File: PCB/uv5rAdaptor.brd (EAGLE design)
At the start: 100 x 80 mm, 2 parts

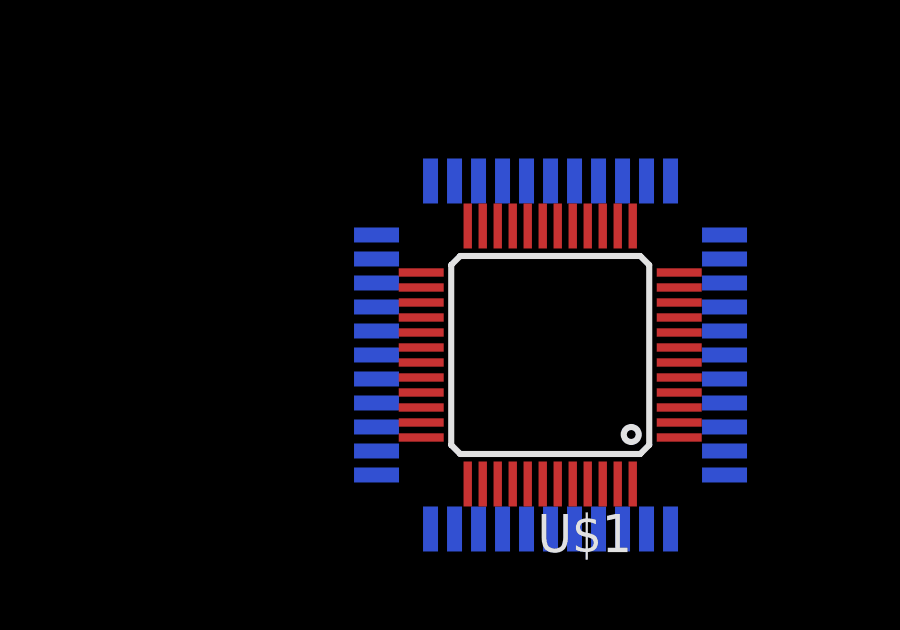
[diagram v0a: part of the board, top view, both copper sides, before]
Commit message: Link all points except for gpio6, we will do that once everything is routed
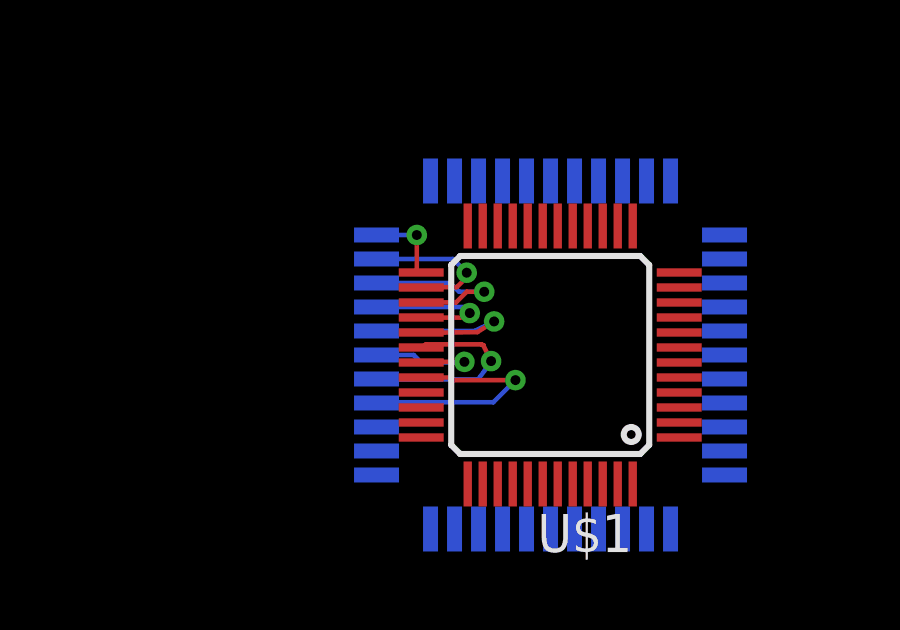
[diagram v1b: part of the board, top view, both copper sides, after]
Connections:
- net N$43 renamed NC1
- net N$45 renamed NC2
- removed net N$1: U$1.1
- removed net N$10: U$1.10
- removed net N$11: U$1.11
- removed net N$12: U$1.12
- removed net N$13: U$1.13
- removed net N$16: U$1.16
- removed net N$17: U$1.17
- removed net N$18: U$1.18
- removed net N$19: U$1.19
- removed net N$20: U$1.20
- removed net N$21: U$1.21
- removed net N$22: U$1.22
- removed net N$30: U$1.25
- removed net N$31: U$1.26
- removed net N$32: U$1.27
- removed net N$33: U$1.28
- removed net N$34: U$1.29
- removed net N$35: U$1.30
- removed net N$36: U$1.31
- removed net N$37: U$1.32
- removed net N$38: U$1.33
- removed net N$39: U$1.34
- removed net N$42: U$1.37
- removed net N$46: U$1.41
- removed net N$48: U$1.43
- new net NC11: U$1.46
- net CLK_FM: now also U$1.18
- net DATA_FM: now also U$1.32
- net GPIO0: now also U$1.17
- net GREEN_LED: now also U$1.43
- net KEY_C4: now also U$1.20; no longer U$1.46
- net KEY_COL1: now also U$1.25
- net KEY_COL2: now also U$1.26; no longer U$1.2
- net KEY_COL3: now also U$1.27; no longer U$1.3
- net LCD_CE: now also U$1.34
- net LCD_DB4: now also U$1.28; no longer U$1.4
- net LCD_DB5: now also U$1.29
- net LCD_RS: now also U$1.33
- net LOW_BAT: now also U$1.1
- net RDX/PPT: now also U$1.22
- net RED_LED: now also U$1.37
- net RX_LED: now also U$1.12
- net RX_PW: now also U$1.19
- net SCK_EEPROM: now also U$1.13
- net SCL_VOICE: now also U$1.16
- net SDA_VOICE: now also U$1.11
- net SDR_SCK: now also U$1.30
- net SDR_SDIO: now also U$1.31
- net SEN: now also U$1.10
- net SPK_AMP: now also U$1.3
- net TXD: now also U$1.21
- net TX_PW: now also U$1.2
- net UHF/VHF: now also U$1.41
- net VOX: now also U$1.4
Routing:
- net DATA_FM: track 0.00 -> 8.13 mm, vias 0 -> 1
- net SDR_SCK: track 0.00 -> 6.85 mm, vias 0 -> 1
- net LCD_DB5: track 0.00 -> 6.53 mm, vias 0 -> 1
- net KEY_COL3: track 0.00 -> 5.99 mm, vias 0 -> 1
- net LCD_DB4: track 0.00 -> 5.16 mm, vias 0 -> 1
- net KEY_COL2: track 0.00 -> 5.00 mm, vias 0 -> 1
- net SDR_SDIO: track 0.00 -> 4.49 mm, vias 0 -> 1
- net KEY_COL1: track 0.00 -> 2.74 mm, vias 0 -> 1

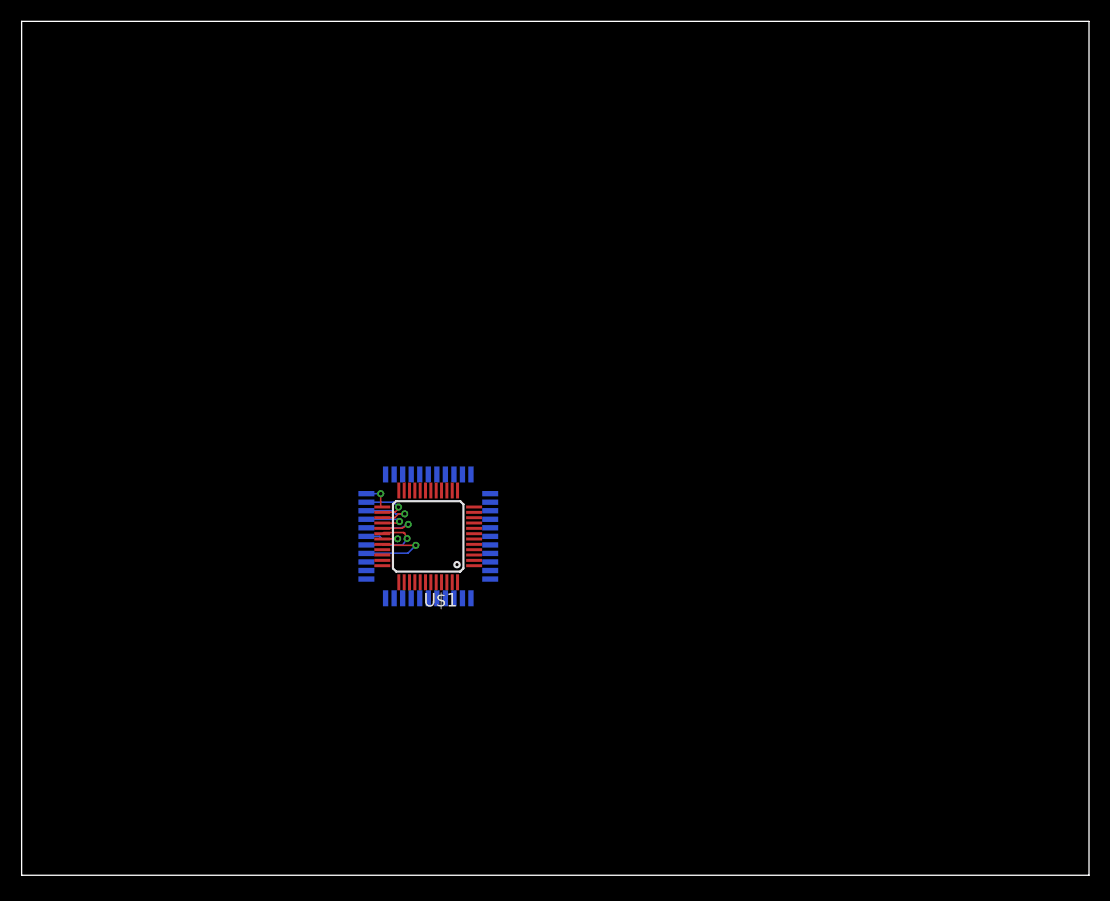
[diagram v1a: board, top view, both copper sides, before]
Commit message: Updated dims
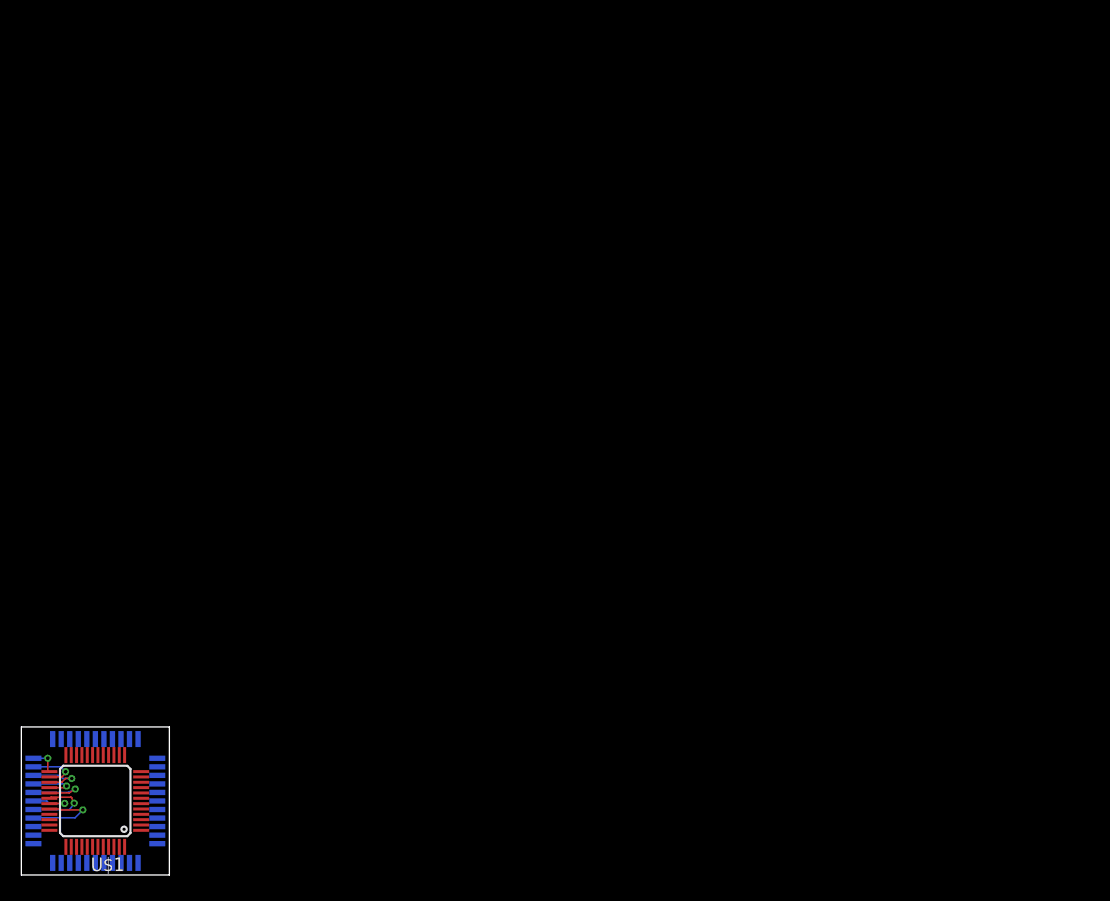
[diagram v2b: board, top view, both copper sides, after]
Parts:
- moved U$1 39.8 mm to (6.90, 6.96)
- moved U$2 39.8 mm to (6.91, 6.96)
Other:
- board size 100 x 80 mm -> 13.9 x 13.9 mm

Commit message: More routing
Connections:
- removed net N$50: U$1.45
- removed net NC1: U$1.38
- removed net NC11: U$1.46
- new net NC3: U$1.2
- new net NC4: U$1.3
- net LED_FL: now also U$1.38
- net SPK_AMP: now also U$1.46; no longer U$1.3
- net TX_PW: now also U$1.45; no longer U$1.2
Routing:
- net RESET: track 0.00 -> 8.11 mm, vias 0 -> 1
- net LCD_RS: track 0.00 -> 7.54 mm, vias 0 -> 1
- net OSC_IN: track 0.00 -> 7.31 mm, vias 0 -> 1
- net OSC_OUT: track 0.00 -> 7.25 mm, vias 0 -> 1
- net TX_PW: track 0.00 -> 6.69 mm, vias 0 -> 1
- net UHF/VHF: track 0.00 -> 6.33 mm, vias 0 -> 1
- net GREEN_LED: track 0.00 -> 6.32 mm, vias 0 -> 1
- net SPK_AMP: track 0.00 -> 6.21 mm, vias 0 -> 1
- net LCD_CE: track 0.00 -> 6.08 mm, vias 0 -> 1
- net VOX: track 0.00 -> 5.76 mm, vias 0 -> 1
- net LOW_BAT: track 0.00 -> 5.51 mm, vias 0 -> 1
- net LED_FL: track 0.00 -> 5.09 mm, vias 0 -> 1
- net RED_LED: track 0.00 -> 3.17 mm, vias 0 -> 1
- net SEN: track 0.00 -> 1.39 mm

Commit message: More traces
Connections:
- net KEY_C4: now also U$1.19; no longer U$1.20
- net RX_PW: now also U$1.20; no longer U$1.19
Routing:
- net VSS: track 0.00 -> 31.4 mm, vias 0 -> 4
- net VDD: track 0.00 -> 24.9 mm, vias 0 -> 1
- net TX_BIAS: track 0.00 -> 16.3 mm, vias 0 -> 1
- net TONE: track 0.00 -> 12.7 mm, vias 0 -> 1
- net GPIO0: track 0.00 -> 9.03 mm, vias 0 -> 1
- net CLK_FM: track 0.00 -> 8.82 mm, vias 0 -> 1
- net AVDD: track 0.00 -> 8.61 mm
- net AVSS: track 0.00 -> 8.36 mm, vias 0 -> 1
- net GREEN_LED: track 6.32 -> 7.99 mm
- net OSC_IN: track 7.31 -> 6.28 mm
- net RESET: track 8.11 -> 7.11 mm

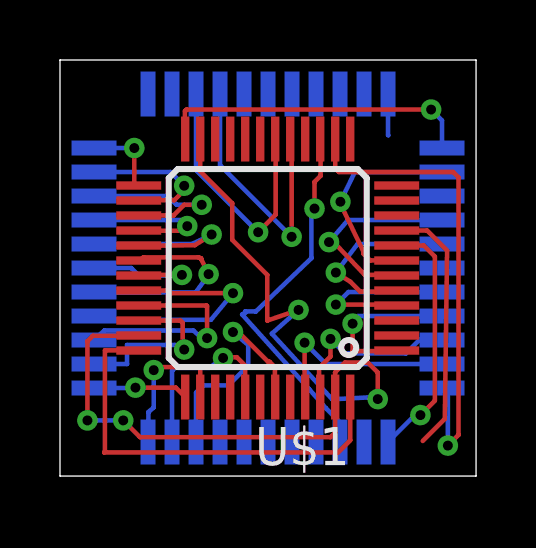
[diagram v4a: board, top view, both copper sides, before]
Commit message: Finished Routing
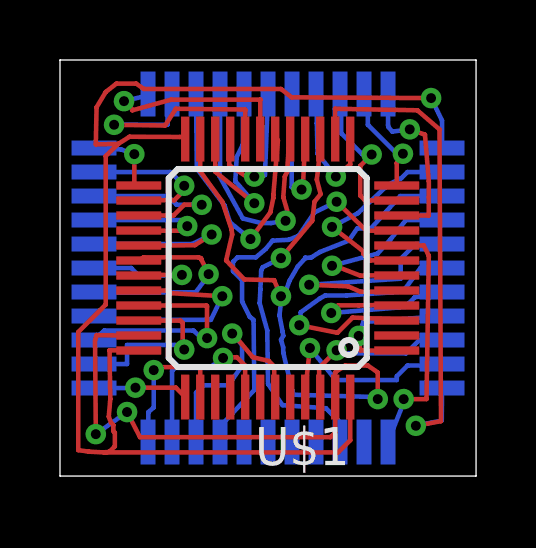
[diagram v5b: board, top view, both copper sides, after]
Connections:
- removed net N$49: U$1.44
- removed net NC3: U$1.2
- new net NC1: U$1.2
- net GPIO6: now also U$1.3
- net NC2: now also U$1.44; no longer U$1.40
- net NC4: now also U$1.40; no longer U$1.3
- net RX_LED: now also U$1.11; no longer U$1.12
- net SDA_VOICE: now also U$1.12; no longer U$1.11
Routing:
- net VDD: track 24.9 -> 43.9 mm
- net GPIO6: track 0.00 -> 9.21 mm, vias 0 -> 1
- net RX_PW: track 0.00 -> 8.52 mm, vias 0 -> 1
- net KEY_C4: track 0.00 -> 6.98 mm, vias 0 -> 1
- net VSS: track 31.4 -> 38.1 mm
- net RDX/PPT: track 0.00 -> 6.71 mm, vias 0 -> 1
- net RX_LED: track 0.00 -> 5.44 mm, vias 0 -> 1
- net SCL_VOICE: track 0.00 -> 5.16 mm, vias 0 -> 1
- net TXD: track 0.00 -> 5.00 mm, vias 0 -> 1
- net AVDD: track 8.61 -> 13.5 mm, vias 0 -> 1
- net SEN: track 1.39 -> 6.20 mm, vias 0 -> 1
- net SCK_EEPROM: track 0.00 -> 4.45 mm, vias 0 -> 1
- net SDA_VOICE: track 0.00 -> 3.85 mm, vias 0 -> 1
- net OSC_IN: track 6.28 -> 8.27 mm
- net TX_BIAS: track 16.3 -> 17.3 mm
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
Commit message: Cleanup Routes
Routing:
- net VSS: track 38.1 -> 36.7 mm, vias 4 -> 2
- net VDD: track 43.9 -> 42.6 mm, vias 1 -> 3
- net TONE: track 12.7 -> 13.6 mm
- net AVDD: track 13.5 -> 13.0 mm
